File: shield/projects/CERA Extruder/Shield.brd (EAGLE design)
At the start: 102.9 x 55.9 mm, 2 parts

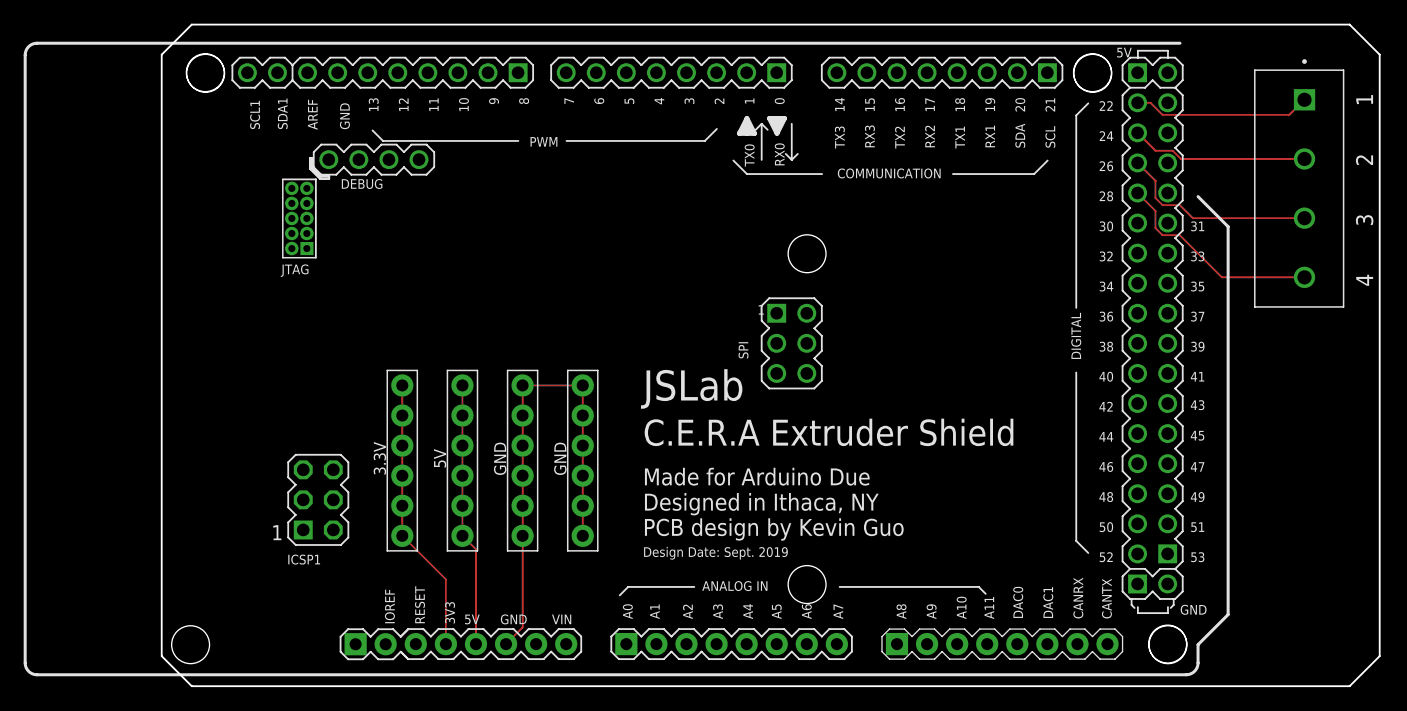
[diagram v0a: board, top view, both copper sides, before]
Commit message: added routing for pins
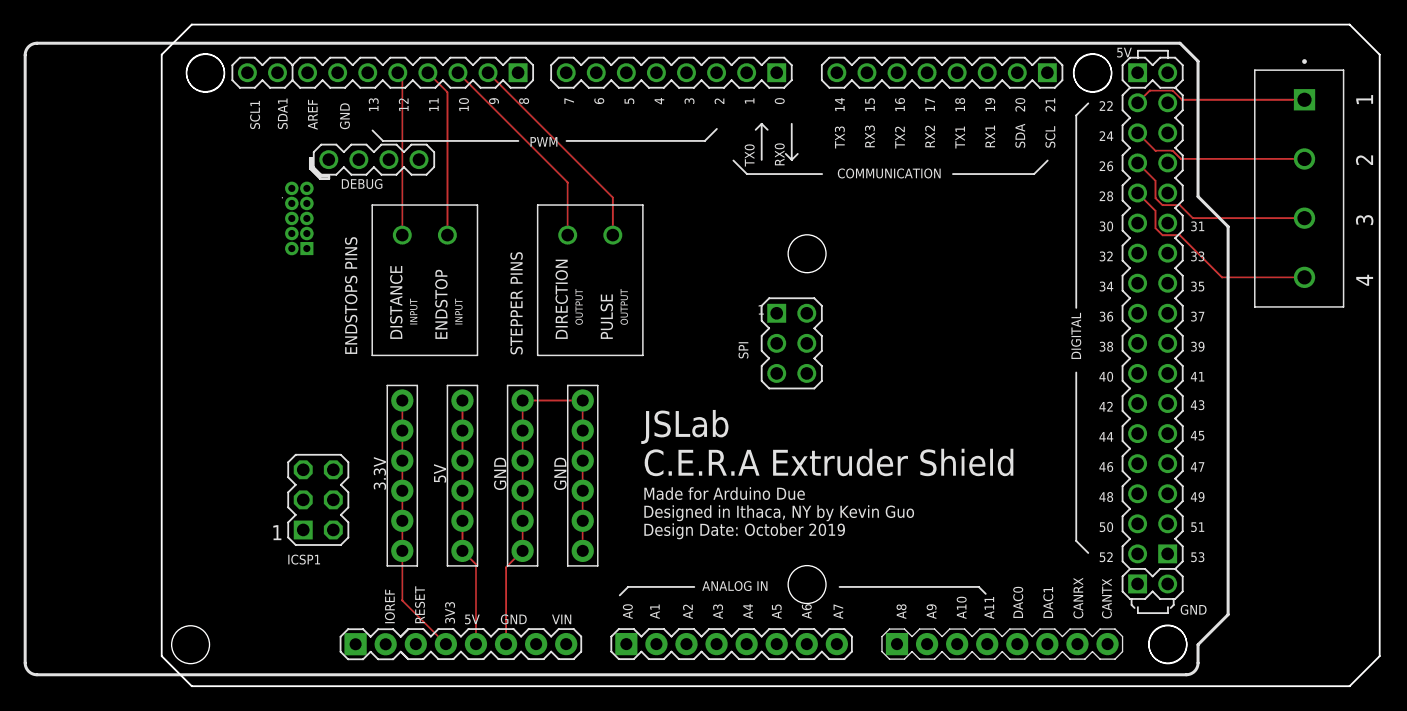
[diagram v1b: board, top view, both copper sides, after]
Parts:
- renumbered E$5 to E$2
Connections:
- new net S$10: E$2.5V0, E$2.5V0X1, E$2.5V0X2, E$2.5V0X3, E$2.5V0X4, E$2.5V0X5, E$2.5V0X6
- new net S$11: E$2.GND, E$2.GNDX1, E$2.GNDX10, E$2.GNDX11, E$2.GNDX12, E$2.GNDX2, E$2.GNDX3, E$2.GNDX4, E$2.GNDX5, E$2.GNDX6, E$2.GNDX7, E$2.GNDX8, E$2.GNDX9
- new net S$8: E$1.4, E$2.28
- new net S$9: E$2.3V3, E$2.3V3X1, E$2.3V3X2, E$2.3V3X3, E$2.3V3X4, E$2.3V3X5, E$2.3V3X6
- net S$1: now also E$2.9, E$2.PULSE; no longer E$2.3V3, E$2.3V3X1, E$2.3V3X2, E$2.3V3X3, E$2.3V3X4, E$2.3V3X5, E$2.3V3X6
- net S$2: now also E$2.10, E$2.DIRECTION; no longer E$2.5V0, E$2.5V0X1, E$2.5V0X2, E$2.5V0X3, E$2.5V0X4, E$2.5V0X5, E$2.5V0X6
- net S$3: now also E$2.11, E$2.ENDSTOP; no longer E$2.GND, E$2.GNDX1, E$2.GNDX10, E$2.GNDX11, E$2.GNDX12, E$2.GNDX2, E$2.GNDX3, E$2.GNDX4, E$2.GNDX5, E$2.GNDX6, E$2.GNDX7, E$2.GNDX8, E$2.GNDX9
- net S$4: now also E$2.12, E$2.DIST; no longer E$1.1, E$2.22
- net S$5: now also E$1.1, E$2.22; no longer E$1.2, E$2.24
- net S$6: now also E$1.2, E$2.24; no longer E$1.3, E$2.26
- net S$7: now also E$1.3, E$2.26; no longer E$1.4, E$2.28
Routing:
- net S$11: track 0.00 -> 38.9 mm
- net S$3: track 40.2 -> 14.4 mm
- net S$9: track 0.00 -> 22.1 mm
- net S$10: track 0.00 -> 21.0 mm
- net S$8: track 0.00 -> 17.9 mm
- net S$1: track 23.4 -> 18.1 mm
- net S$2: track 22.3 -> 17.6 mm
- net S$6: track 16.9 -> 15.0 mm
- net S$4: track 15.1 -> 13.9 mm
- net S$7: track 17.9 -> 16.9 mm
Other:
- board text removed: "C.E.R.A Extruder Shield"
- board text removed: "Design Date: Sept. 2019"
- board text removed: "JSLab"
- board text removed: "Made for Arduino Due Designed in Ithaca, NY PCB design by Kevin Guo"
